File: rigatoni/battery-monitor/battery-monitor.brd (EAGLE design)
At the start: 69.8 x 133.3 mm, 56 parts, among them J1 S2B-XH-A_(LF)(SN), J4 S4B-XH-A(LF)(SN), J5 S2B-XH-A_(LF)(SN), J6 S4B-XH-A(LF)(SN), Q1 STT4P3LLH6, Q2 BSS138, Q3 BSS138, Q4 BSS138, Q5 BSS138, U1 LT1930ES5TRMPBF_BOOST_CONV, U2 NUCLEO-H743ZI-HEADER, U3 TPSM84205EAB

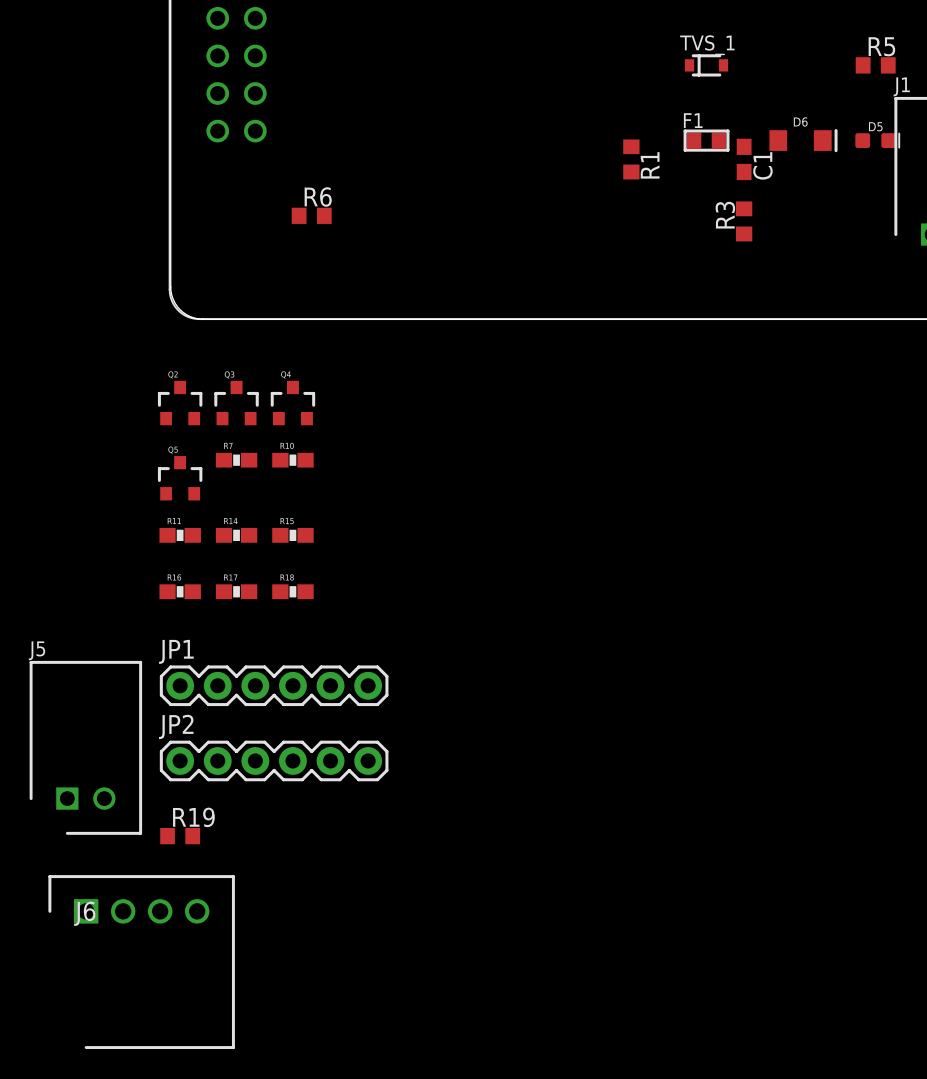
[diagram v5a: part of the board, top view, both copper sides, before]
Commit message: Implemented changes from schematic review
LED Connector and Power Circuitry still needs to be updated in schematic
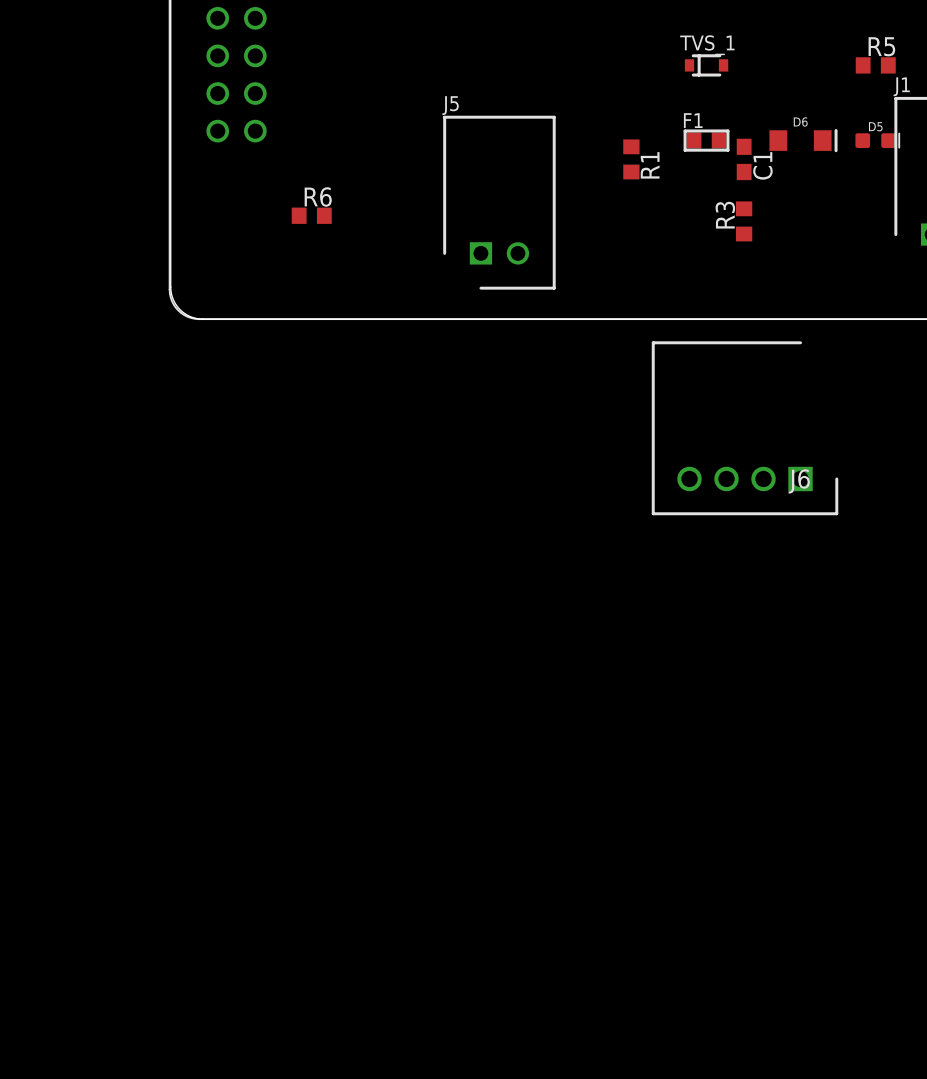
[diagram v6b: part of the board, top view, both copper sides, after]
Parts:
- removed JP1, JP2: (no value), SparkFun:1X06
- removed Q2, Q3, Q4, Q5: BSS138, SparkFun:SOT23-3
- removed R10, R11, R14, R15, R16, R17, R18, R7: 10K, SparkFun:0603-RES
- removed R19: 1k, rcl:R0603
- C1: value 1 uF -> 47 uF
- R1: value 5 kΩ -> 20 kΩ
- R3: value 55 kΩ -> 350 kΩ
- moved J6 56.4 mm to (69.8, -38.1), turned to 180 degrees
- moved J5 46.2 mm to (49.5, -19.1)
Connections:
- removed net GND_CN7: U2.CN7_8
- removed net GND_CN9: U2.CN9_12, U2.CN9_23
- removed net HV: JP2.3, R10.1, R14.1, R16.1, R18.1
- removed net HV1: JP2.1, Q3.3, R14.2
- removed net HV2: JP2.2, Q4.3, R16.2
- removed net HV3: JP2.5, Q5.3, R18.2
- removed net HV4: JP2.6, Q2.3, R10.2
- removed net LV: JP1.4, Q2.1, Q3.1, Q4.1, Q5.1, R11.1, R15.1, R17.1, R7.1
- removed net LV1: JP1.6, Q3.2, R11.2
- removed net LV2: JP1.5, Q4.2, R15.2
- removed net LV3: JP1.2, Q5.2, R17.2
- removed net LV4: JP1.1, Q2.2, R7.2
- net GND: now also U2.CN7_8, U2.CN9_12, U2.CN9_23; no longer JP1.3, JP2.4
- net N$2: no longer R19.1

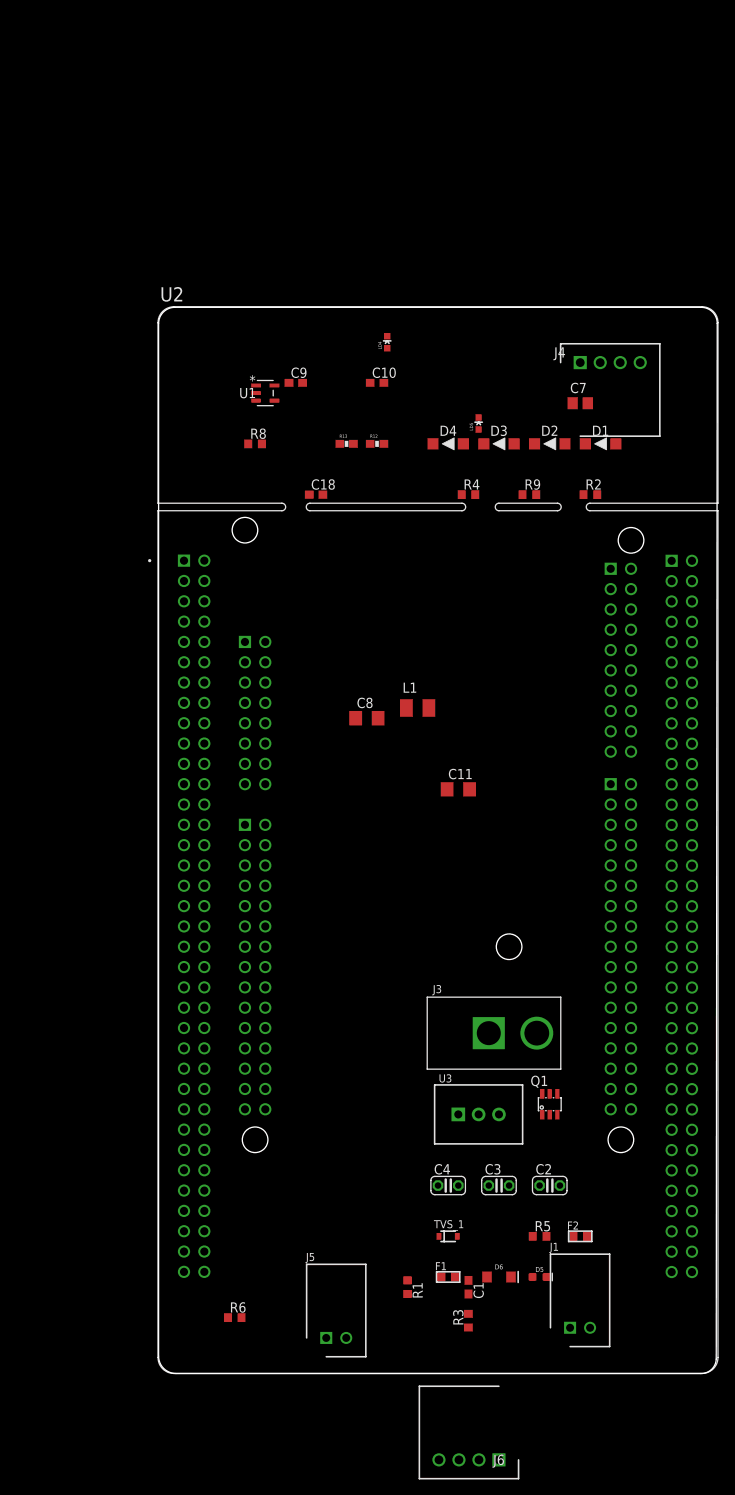
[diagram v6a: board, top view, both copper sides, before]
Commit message: Started routing the board
LED connector still not completed
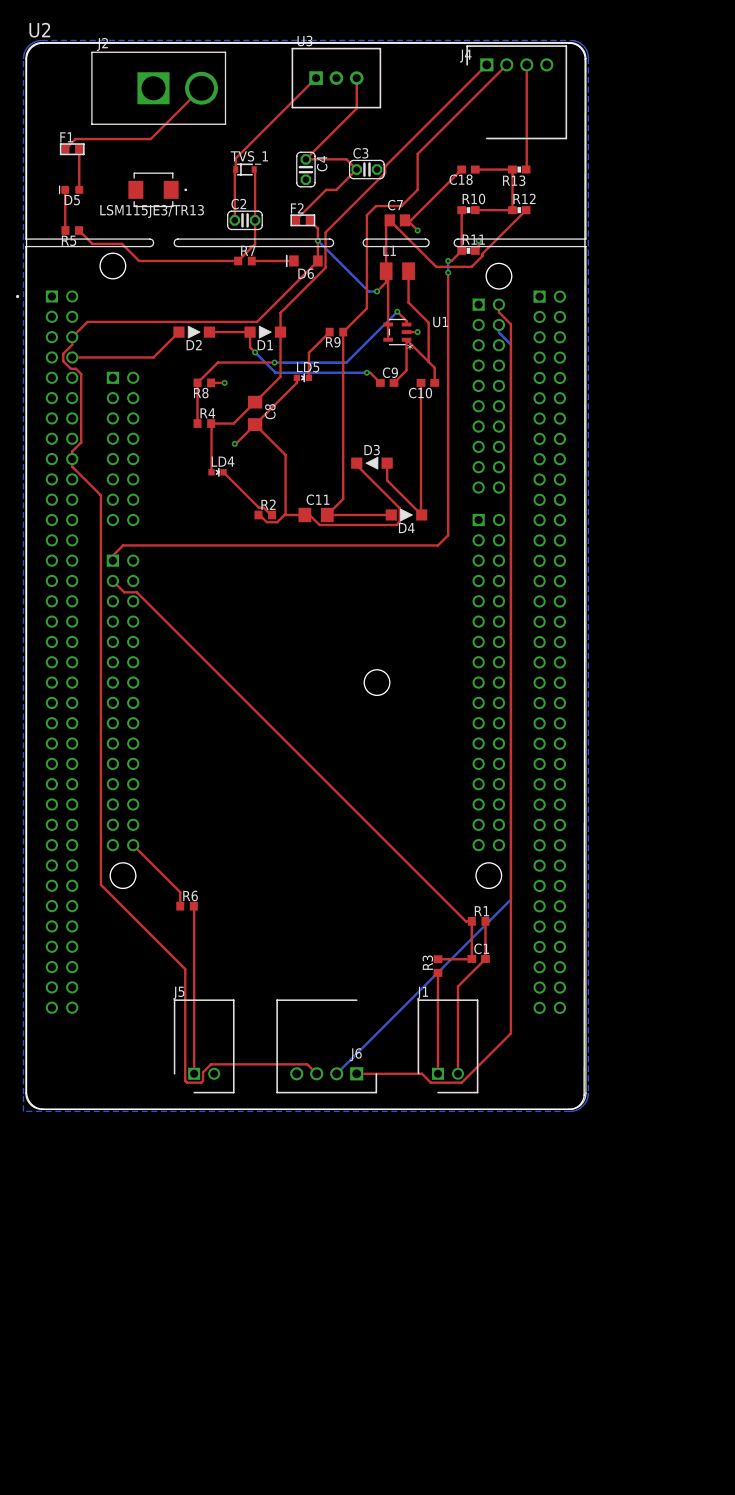
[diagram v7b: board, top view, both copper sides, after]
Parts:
- removed J3: (no value), RoboJackets-Connectors:PJ-037A
- removed Q1: STT4P3LLH6, RoboJackets-Discrete:SOT23-6
- added CR1: LSM115JE3/TR13, RoboRacing_STM:DO-214BA_MCH
- added J2: (no value), RoboJackets-Connectors:PJ-037A
- added R10: 50kΩ, SparkFun:0603-RES
- added R11: 100kΩ, SparkFun:0603-RES
- added R7: 150R, rcl:R0603
- C4: value 100uF -> 47uF
- R5: value 1k -> 500R
- moved F1 148.6 mm to (16.5, 125.7)
- moved D5 147.9 mm to (16.5, 120.7), turned to 180 degrees
- moved R5 138.6 mm to (16.5, 115.6), turned to 180 degrees
- moved TVS_1 135.7 mm to (38.1, 123.2)
- moved F2 131.6 mm to (45.3, 116.8)
- moved U3 130.8 mm to (49.5, 134.6)
- moved D6 129.3 mm to (45.7, 111.8), turned to 180 degrees
- moved C4 128.2 mm to (45.7, 123.2), turned to 270 degrees
- moved C3 128.1 mm to (53.3, 123.2)
- moved C2 126.5 mm to (38.1, 116.8)
- moved L1 54.7 mm to (57.1, 110.5)
- moved R6 51.8 mm to (30.9, 31.1)
- moved J6 51.4 mm to (52.1, 10.2)
- moved D2 46.6 mm to (31.8, 102.9), turned to 180 degrees
- moved R1 46.6 mm to (67.3, 29.2), turned to 0 degrees
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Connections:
- removed net GND_CN10: U2.CN10_17, U2.CN10_22, U2.CN10_27, U2.CN10_5
- removed net GND_CN12: U2.CN12_20, U2.CN12_39, U2.CN12_54, U2.CN12_63, U2.CN12_71, U2.CN12_72, U2.CN12_9
- removed net GND_CN8: U2.CN8_11, U2.CN8_13
- new net N$10: D6.C, R7.2
- net +5V: no longer C3.1, D6.C
- net 5V_MAIN: now also C3.1
- net CURR_DATA: now also R10.1, R10.2, R11.1
- net GND: now also J2.P$1, R11.2, R7.1, U2.CN10_17, U2.CN10_22, U2.CN10_27, U2.CN10_5, U2.CN12_20, U2.CN12_39, U2.CN12_54, U2.CN12_63, U2.CN12_71, U2.CN12_72, U2.CN12_9, U2.CN8_11, U2.CN8_13; no longer J3.P$1
- net N$2: now also CR1.2; no longer D5.C, Q1.1, Q1.2, Q1.5, Q1.6
- net N$3: now also C2.1, CR1.1, TVS_1.C, U3.VIN; no longer Q1.3, R5.2
- net N$4: now also F1.1, J2.P$2; no longer C2.1, Q1.4, TVS_1.C, U3.VIN
- net N$7: now also D5.C, R5.2; no longer F1.1, J3.P$2
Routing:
- net +5V: track 0.00 -> 210.6 mm, vias 0 -> 2
- net GND: track 0.00 -> 138.4 mm, vias 0 -> 5
- net I2C_SCL: track 0.00 -> 114.0 mm
- net I2C_SDA: track 0.00 -> 103.2 mm
- net CURR_DATA: track 0.00 -> 99.6 mm, vias 0 -> 2
- net -15V: track 0.00 -> 75.4 mm
- net VOLT_DATA: track 0.00 -> 71.4 mm
- net +15V: track 0.00 -> 66.9 mm
- net N$5: track 0.00 -> 35.8 mm, vias 0 -> 2
- net 5V_MAIN: track 0.00 -> 29.9 mm
- net N$6: track 0.00 -> 25.3 mm
- net N$16: track 0.00 -> 25.1 mm, vias 0 -> 2
- net N$8: track 0.00 -> 24.8 mm
- net N$3: track 0.00 -> 22.0 mm
- net N$9: track 0.00 -> 21.0 mm
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- added copper zone on layer 16, net GND

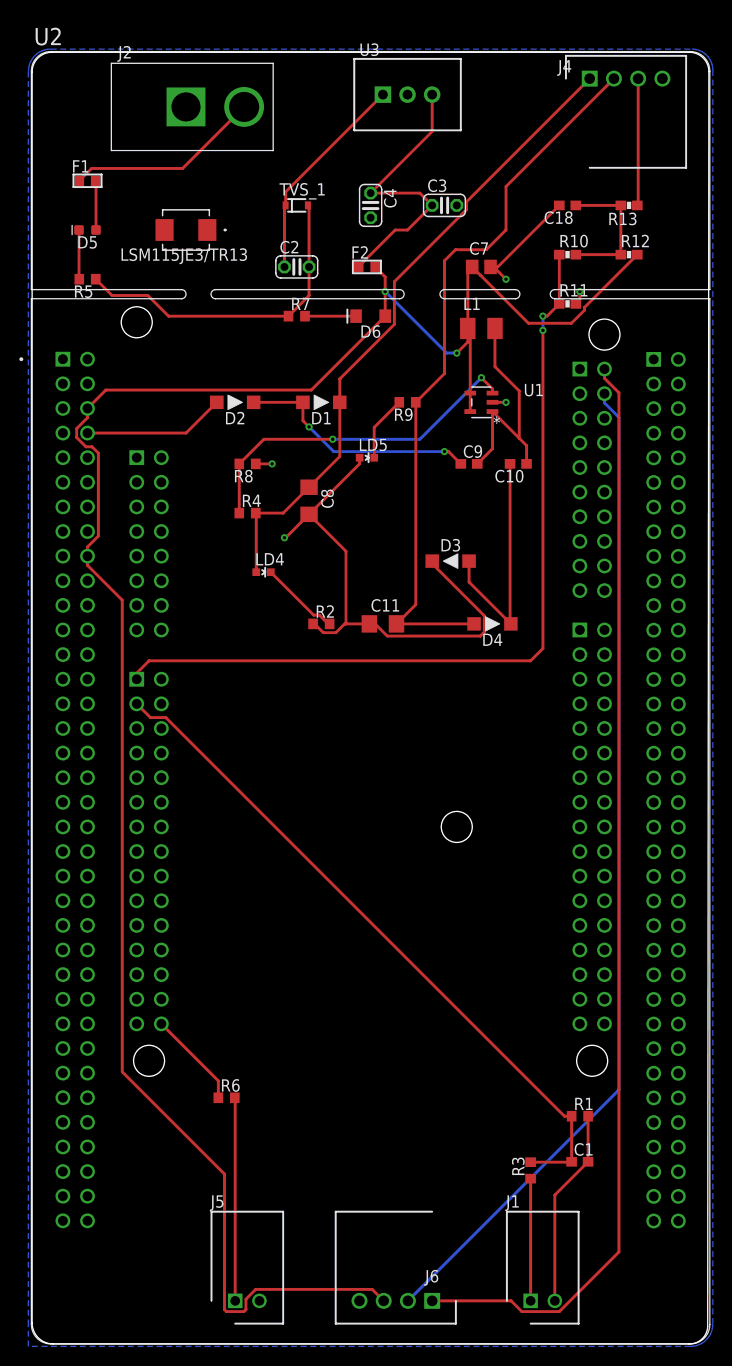
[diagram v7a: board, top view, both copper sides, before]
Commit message: Completed routing for v1.0
Removed LED connector and ready for design review
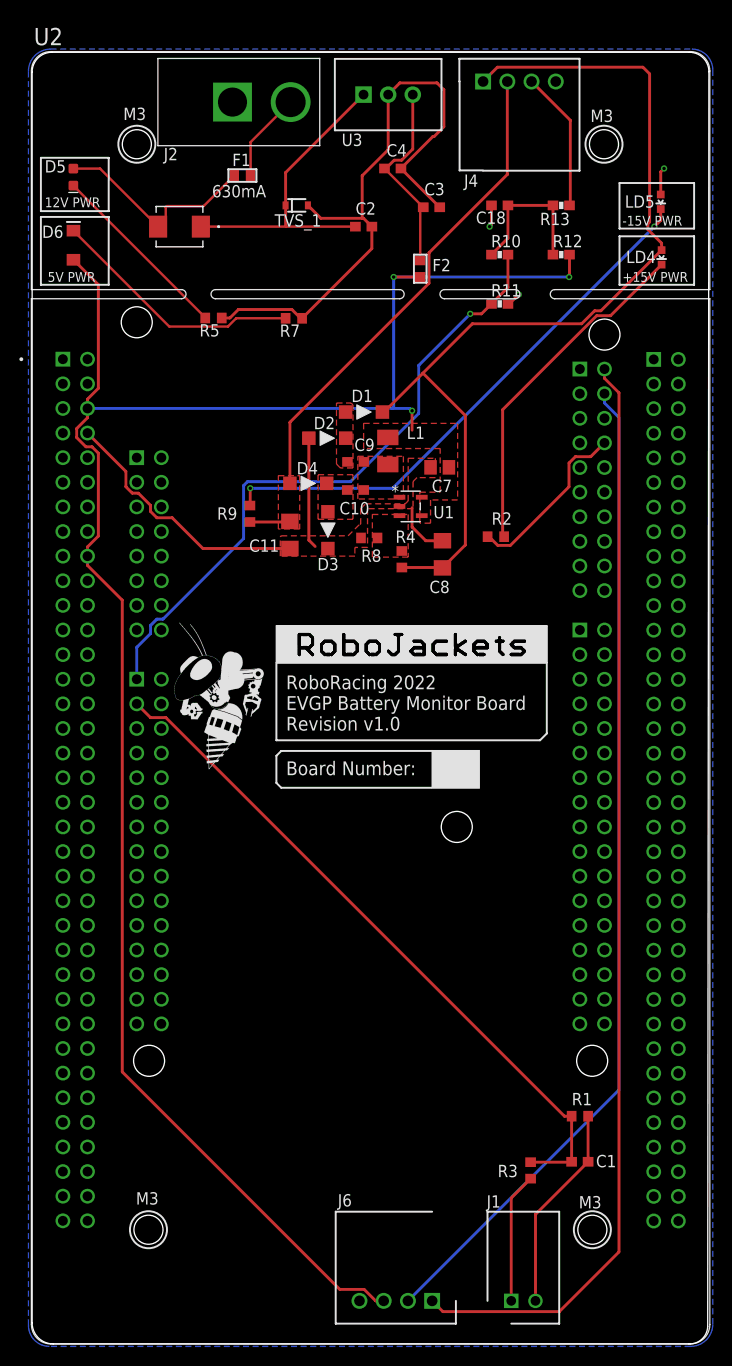
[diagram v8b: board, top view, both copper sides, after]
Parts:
- removed J5: S2B-XH-A_(LF)(SN), drive_brake:SHDR2W80P0X250_1X2_740X1150X61
- removed R6: 220 Ω, rcl:R0603
- added U$1: (no value), RoboJackets-Aesthetics:ROBOBUZZ_0.8X
- added U$2: (no value), RoboJackets-Aesthetics:ROBOJACKETS
- C2: value 10uF -> 10 uF; device rcl:C025-024X044 -> rcl:C0603
- C3: value 0.1uF -> 0.1 uF; device rcl:C025-024X044 -> rcl:C0603
- C4: value 47uF -> 47 uF; device rcl:C025-024X044 -> rcl:C0603
- D5: value Yellow -> YELLOW
- R5: value 500R -> 500Ω
- R7: value 150R -> 150Ω
- moved LD4 52.4 mm to (75.7, 117.8), turned to 180 degrees
- moved LD5 40.2 mm to (75.7, 123.6), turned to 180 degrees
- moved D6 31.5 mm to (15.1, 119.1), turned to 90 degrees
- moved D4 23.9 mm to (39.3, 94.5)
- moved C7 21.1 mm to (52.9, 96.2), turned to 180 degrees
- moved R2 20.1 mm to (58.6, 89.0)
- moved R9 19.9 mm to (33.3, 91.4), turned to 90 degrees
- moved C10 17.0 mm to (44.2, 93.8)
- moved R4 16.6 mm to (48.9, 86.7), turned to 270 degrees
- moved F1 16.0 mm to (32.5, 126.3), turned to 180 degrees
- moved L1 15.9 mm to (47.5, 97.8), turned to 270 degrees
- moved C8 14.8 mm to (53.1, 87.2), turned to 90 degrees
- moved R8 14.7 mm to (45.6, 88.9), turned to 0 degrees
- moved R5 13.6 mm to (29.5, 111.6)
- moved C11 13.3 mm to (37.4, 89.2), turned to 90 degrees
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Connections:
- removed net LED: R6.1, U2.CN9_30
- removed net N$9: J5.1, R6.2
- new net N$11: C18.1, R10.1, R12.1, R13.2
- net CURR_DATA: no longer C18.1, R10.1, R12.1, R13.2
- net GND: no longer J5.2
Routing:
- net N$17: track 6.79 -> 56.8 mm, vias 0 -> 2
- net N$5: track 35.8 -> 0.00 mm, vias 2 -> 0
- net +15V: track 66.9 -> 99.7 mm
- net CURR_DATA: track 99.6 -> 66.9 mm, vias 2 -> 1
- net N$14: track 8.28 -> 35.9 mm
- net N$6: track 25.3 -> 0.00 mm
- net N$16: track 25.1 -> 0.00 mm, vias 2 -> 0
- net N$8: track 24.8 -> 0.00 mm
- net N$10: track 5.27 -> 26.3 mm
- net N$9: track 21.0 -> 0.00 mm
- net -15V: track 75.4 -> 54.9 mm
- net GND: track 138.4 -> 155.5 mm, vias 5 -> 3
- net N$2: track 5.09 -> 22.0 mm
- net N$11: track 0.00 -> 15.5 mm
- net N$7: track 5.09 -> 19.3 mm
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- added copper zone on layer 1, net +5V
- added copper zone on layer 1, net -15V
- added copper zone on layer 1, net GND
- added copper zone on layer 1, net N$16
- added copper zone on layer 1, net N$5
- added copper zone on layer 1, net N$6
- added copper zone on layer 1, net N$8
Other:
- board text added: "+15V PWR"
- board text added: "-15V PWR"
- board text added: "12V PWR"
- board text added: "5V PWR"
- board text added: "Board Number:"
- board text added: "M3"
- board text added: "RoboRacing 2022 EVGP Battery Monitor Board Revision v1.0"
